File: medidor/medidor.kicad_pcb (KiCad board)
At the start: 2 copper layers, 55 x 80 mm, 23 parts, among them J1 Screw_Terminal_01x02, J2 Conn_01x01_Female, J3 Conn_01x01_Female, J4 Conn_01x06, J5 Screw_Terminal_01x02, U1 LTC1966CMS8PBF, U2 MCP6001U

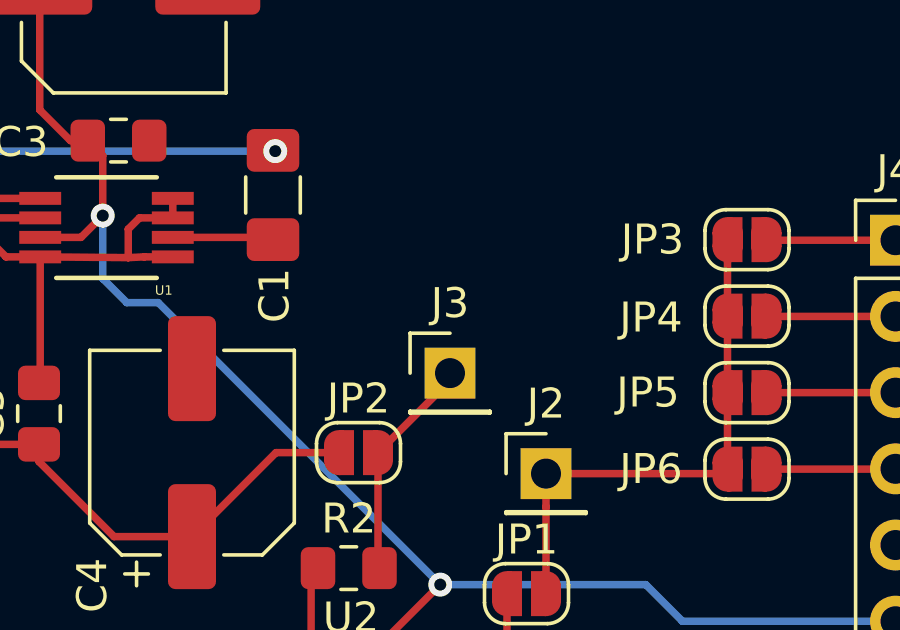
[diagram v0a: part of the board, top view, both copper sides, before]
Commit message: Se agregan cotas al PCB
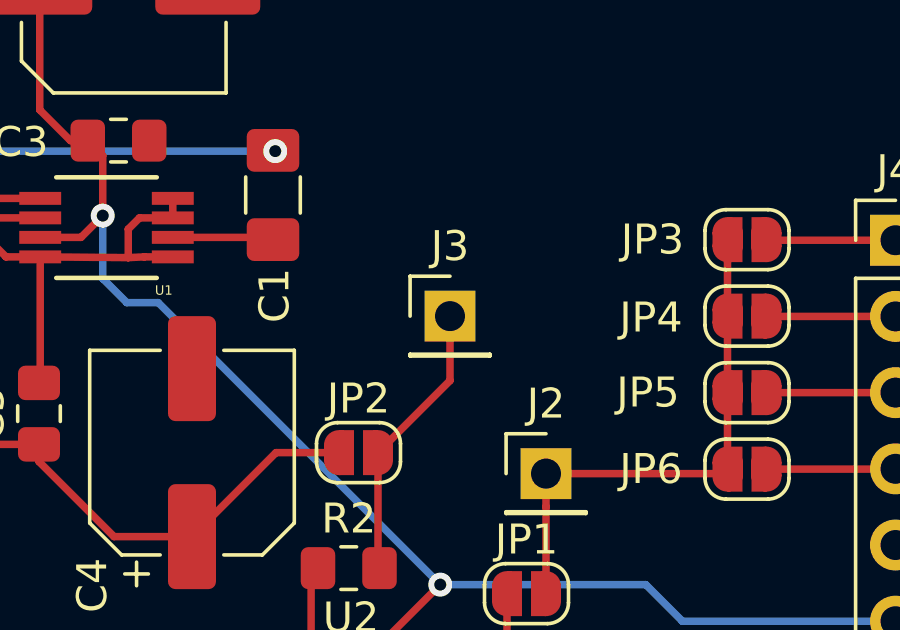
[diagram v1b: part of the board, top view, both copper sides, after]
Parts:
- moved J3 1.90 mm to (135.9, 93.5)
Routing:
- net /IN+_MCP6001: track 7.51 -> 9.41 mm
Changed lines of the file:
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@@
   (general
     (thickness 1.6)
-    (drawings 5)
+    (drawings 7)
     (tracks 94)
     (zones 0)
@@
   )
   (module Connector_PinHeader_2.54mm:PinHeader_1x01_P2.54mm_Vertical (layer F.Cu)
-    (at 135.875 95.35)
+    (at 135.875 93.45)
     (descr "Through hole straight pin header, 1x01, 2.54mm pitch, single row")
     (tags "Through hole pin header THT 1x01 2.54mm single row")
@@
       (rotate (xyz 0 0 0))
     )
+  )
+  (dimension 55 (width 0.15) (layer Dwgs.User)
+    (gr_text "55,000 mm" (at 127.5 43.7) (layer Dwgs.User)
+      (effects (font (size 1 1) (thickness 0.15)))
+    )
+    (feature1 (pts (xy 155 55) (xy 155 44.413579)))
+    (feature2 (pts (xy 100 55) (xy 100 44.413579)))
+    (crossbar (pts (xy 100 45) (xy 155 45)))
+    (arrow1a (pts (xy 155 45) (xy 153.873496 45.586421)))
+    (arrow1b (pts (xy 155 45) (xy 153.873496 44.413579)))
+    (arrow2a (pts (xy 100 45) (xy 101.126504 45.586421)))
+    (arrow2b (pts (xy 100 45) (xy 101.126504 44.413579)))
+  )
+  (dimension 80 (width 0.15) (layer Dwgs.User)
+    (gr_text "80,000 mm" (at 166.3 95 90) (layer Dwgs.User)
+      (effects (font (size 1 1) (thickness 0.15)))
+    )
+    (feature1 (pts (xy 155 55) (xy 165.586421 55)))
+    (feature2 (pts (xy 155 135) (xy 165.586421 135)))
+    (crossbar (pts (xy 165 135) (xy 165 55)))
+    (arrow1a (pts (xy 165 55) (xy 165.586421 56.126504)))
+    (arrow1b (pts (xy 165 55) (xy 164.413579 56.126504)))
+    (arrow2a (pts (xy 165 135) (xy 165.586421 133.873496)))
+    (arrow2b (pts (xy 165 135) (xy 164.413579 133.873496)))
   )
   (gr_text "ENTRADA TI" (at 136.8 73.65) (layer F.SilkS)
@@
   (segment (start 133.475 101.8) (end 133.525 101.85) (width 0.25) (layer F.Cu) (net 6))
   (segment (start 133.475 98) (end 133.475 101.8) (width 0.25) (layer F.Cu) (net 6))
-  (segment (start 135.875 95.6) (end 135.875 95.35) (width 0.25) (layer F.Cu) (net 6))
+  (segment (start 135.875 95.6) (end 135.875 93.45) (width 0.25) (layer F.Cu) (net 6))
   (segment (start 133.475 98) (end 135.875 95.6) (width 0.25) (layer F.Cu) (net 6))
   (segment (start 133.905 106.15) (end 136.575 106.15) (width 0.25) (layer F.Cu) (net 7))

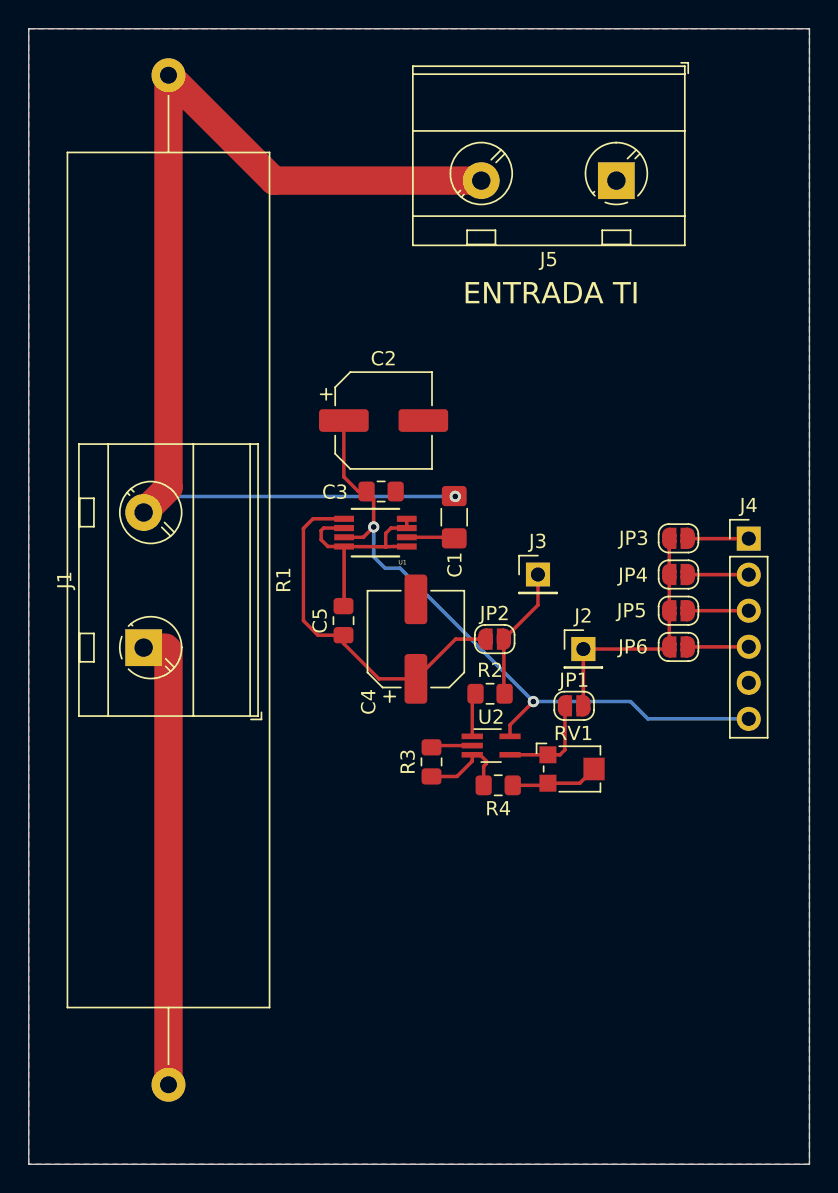
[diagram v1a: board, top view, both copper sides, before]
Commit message: Se agregan fiduciarios
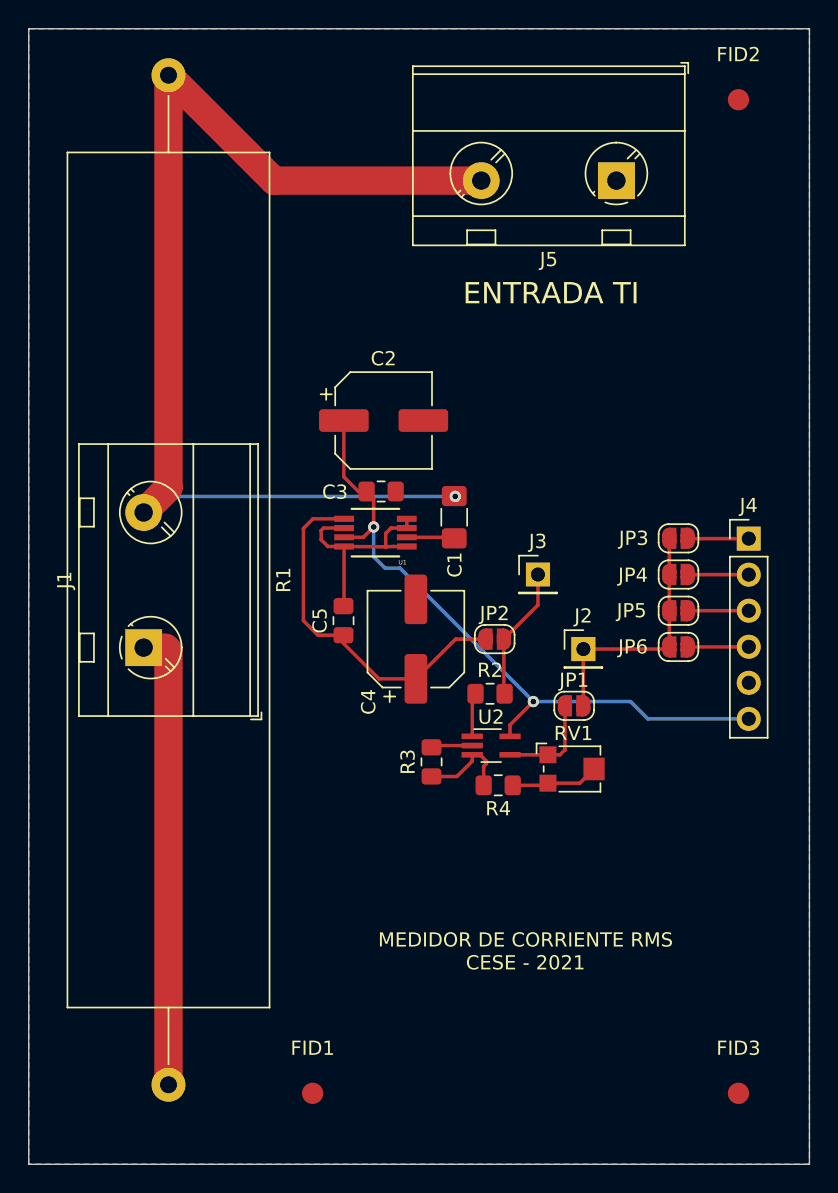
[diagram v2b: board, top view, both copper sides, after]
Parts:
- added FID1: Fiducial, Fiducial:Fiducial_1.5mm_Mask4.5mm, F.Cu at (120.0, 130.0)
- added FID2: Fiducial, Fiducial:Fiducial_1.5mm_Mask4.5mm, F.Cu at (150.0, 60.0)
- added FID3: Fiducial, Fiducial:Fiducial_1.5mm_Mask4.5mm, F.Cu at (150.0, 130.0)
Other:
- board text added: "MEDIDOR DE CORRIENTE RMS CESE - 2021"
- board text added: "NOTAS AL FABRICANTE"
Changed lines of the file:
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@@
   (general
     (thickness 1.6)
-    (drawings 7)
+    (drawings 9)
     (tracks 94)
     (zones 0)
-    (modules 23)
+    (modules 26)
     (nets 16)
   )
@@
     (add_net "Net-(R4-Pad1)")
     (add_net VDD)
+  )
+  (module Fiducial:Fiducial_1.5mm_Mask4.5mm (layer F.Cu)
+    (at 150 130)
+    (descr "Circular Fiducial, 1.5mm bare copper, 4.5mm soldermask opening")
+    (tags fiducial)
+    (attr smd)
+    (fp_text reference FID3 (at 0 -3.175) (layer F.SilkS)
+      (effects (font (size 1 1) (thickness 0.15)))
+    )
+    (fp_text value Fiducial (at 0 3.175) (layer F.Fab)
+      (effects (font (size 1 1) (thickness 0.15)))
+    )
+    (fp_circle (center 0 0) (end 2.5 0) (layer F.CrtYd) (width 0.05))
+    (fp_text user %R (at 0 0) (layer F.Fab)
+      (effects (font (size 0.4 0.4) (thickness 0.06)))
+    )
+    (fp_circle (center 0 0) (end 2.25 0) (layer F.Fab) (width 0.1))
+    (pad "" smd circle (at 0 0) (size 1.5 1.5) (layers F.Cu F.Mask)
+      (solder_mask_margin 1.5) (clearance 1.5))
+  )
+  (module Fiducial:Fiducial_1.5mm_Mask4.5mm (layer F.Cu)
+    (at 150 60)
+    (descr "Circular Fiducial, 1.5mm bare copper, 4.5mm soldermask opening")
+    (tags fiducial)
+    (attr smd)
+    (fp_text reference FID2 (at 0 -3.175) (layer F.SilkS)
+      (effects (font (size 1 1) (thickness 0.15)))
+    )
+    (fp_text value Fiducial (at 0 3.175) (layer F.Fab)
+      (effects (font (size 1 1) (thickness 0.15)))
+    )
+    (fp_circle (center 0 0) (end 2.5 0) (layer F.CrtYd) (width 0.05))
+    (fp_text user %R (at 0 0) (layer F.Fab)
+      (effects (font (size 0.4 0.4) (thickness 0.06)))
+    )
+    (fp_circle (center 0 0) (end 2.25 0) (layer F.Fab) (width 0.1))
+    (pad "" smd circle (at 0 0) (size 1.5 1.5) (layers F.Cu F.Mask)
+      (solder_mask_margin 1.5) (clearance 1.5))
+  )
+  (module Fiducial:Fiducial_1.5mm_Mask4.5mm (layer F.Cu)
+    (at 120 130)
+    (descr "Circular Fiducial, 1.5mm bare copper, 4.5mm soldermask opening")
+    (tags fiducial)
+    (attr smd)
+    (fp_text reference FID1 (at 0 -3.175) (layer F.SilkS)
+      (effects (font (size 1 1) (thickness 0.15)))
+    )
+    (fp_text value Fiducial (at 0 3.175) (layer F.Fab)
+      (effects (font (size 1 1) (thickness 0.15)))
+    )
+    (fp_circle (center 0 0) (end 2.5 0) (layer F.CrtYd) (width 0.05))
+    (fp_text user %R (at 0 0) (layer F.Fab)
+      (effects (font (size 0.4 0.4) (thickness 0.06)))
+    )
+    (fp_circle (center 0 0) (end 2.25 0) (layer F.Fab) (width 0.1))
+    (pad "" smd circle (at 0 0) (size 1.5 1.5) (layers F.Cu F.Mask)
+      (solder_mask_margin 1.5) (clearance 1.5))
   )
   (module TerminalBlock_MetzConnect:TerminalBlock_MetzConnect_Type703_RT10N02HGLU_1x02_P9.52mm_Horizontal (layer F.Cu)
@@
       (rotate (xyz 0 0 0))
     )
+  )
+  (gr_text "MEDIDOR DE CORRIENTE RMS\nCESE - 2021\n" (at 135 120) (layer F.SilkS)
+    (effects (font (size 1 1) (thickness 0.15)))
+  )
+  (gr_text "NOTAS AL FABRICANTE\n" (at 180 70) (layer Dwgs.User)
+    (effects (font (size 1 1) (thickness 0.15)))
   )
   (dimension 55 (width 0.15) (layer Dwgs.User)
@@
   (segment (start 117.27 65.7) (end 109.845 58.275) (width 2) (layer F.Cu) (net 15))
   (segment (start 131.88 65.7) (end 117.27 65.7) (width 2) (layer F.Cu) (net 15))
-  (zone (net 2) (net_name GND) (layer B.Cu) (hatch edge 0.508)
+  (zone (net 2) (net_name GND) (layer F.Cu) (hatch edge 0.508)
     (connect_pads (clearance 0.508))
     (min_thickness 0.254)
@@
     )
   )
-  (zone (net 2) (net_name GND) (layer F.Cu) (hatch edge 0.508)
+  (zone (net 2) (net_name GND) (layer B.Cu) (hatch edge 0.508)
     (connect_pads (clearance 0.508))
     (min_thickness 0.254)

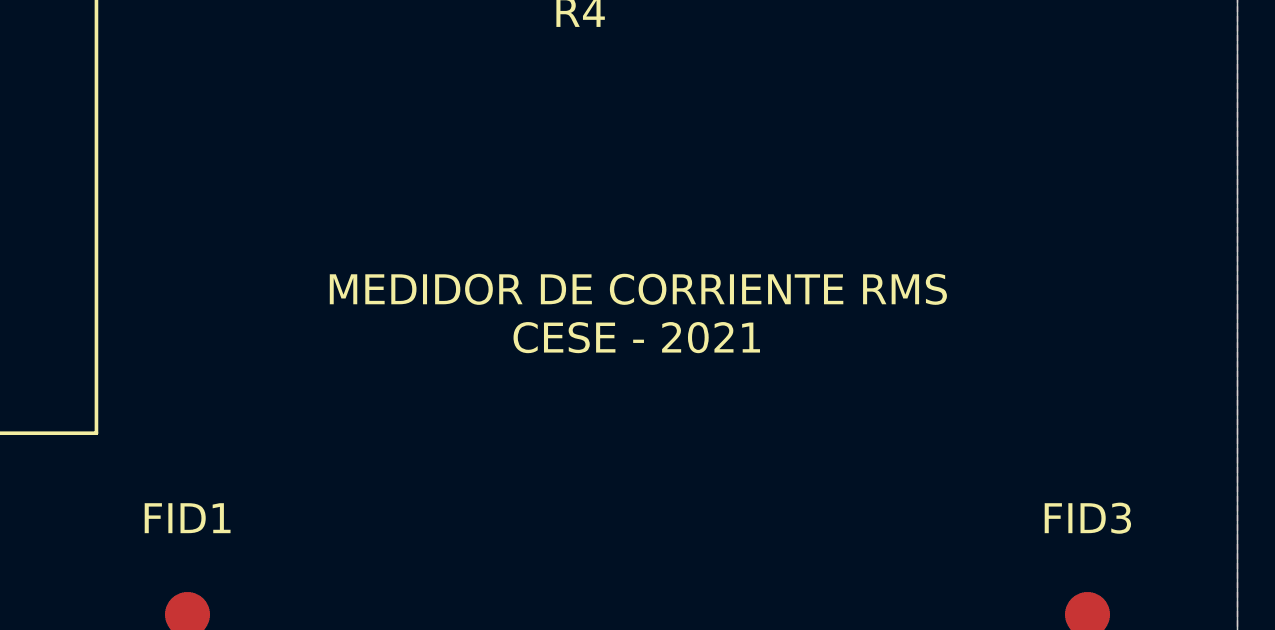
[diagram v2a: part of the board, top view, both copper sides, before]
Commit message: Se agrega leyenda en serigrafia
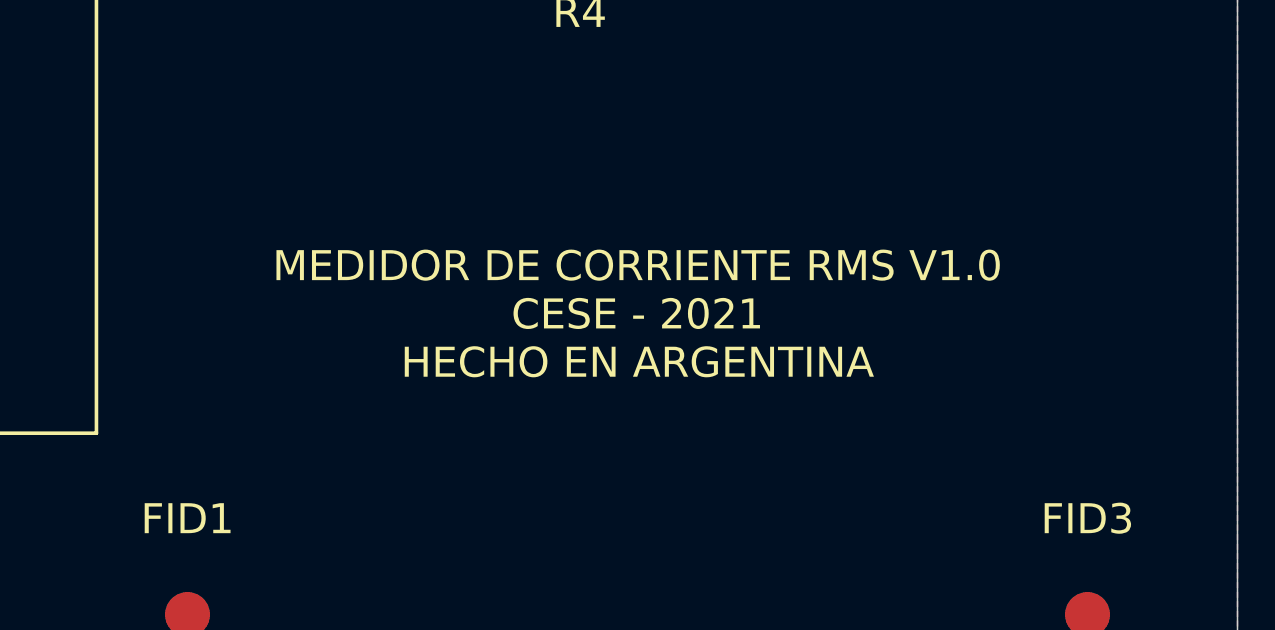
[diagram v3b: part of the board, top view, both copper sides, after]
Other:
- board text added: "MEDIDOR DE CORRIENTE RMS V1.0 CESE - 2021 HECHO EN ARGENTINA"
- board text removed: "MEDIDOR DE CORRIENTE RMS CESE - 2021"
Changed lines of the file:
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@@
     )
   )
-  (gr_text "MEDIDOR DE CORRIENTE RMS\nCESE - 2021\n" (at 135 120) (layer F.SilkS)
+  (gr_text "MEDIDOR DE CORRIENTE RMS V1.0\nCESE - 2021\nHECHO EN ARGENTINA\n" (at 135 120) (layer F.SilkS)
     (effects (font (size 1 1) (thickness 0.15)))
   )
@@
   (segment (start 122.2 82.6) (end 122.2 86.575) (width 0.25) (layer F.Cu) (net 3))
   (segment (start 133.905 104.045) (end 135.55 102.4) (width 0.25) (layer F.Cu) (net 3))
-  (via (at 135.55 102.4) (size 0.8) (drill 0.4) (layers F.Cu B.Cu) (net 3))
+  (via (at 135.55 102.4) (size 0.8) (drill 0.4) (layers F.Cu B.Cu) (net 3) (status 1000000))
   (segment (start 133.905 104.85) (end 133.905 104.045) (width 0.25) (layer F.Cu) (net 3))
   (segment (start 135.55 102.4) (end 126.15 93) (width 0.25) (layer B.Cu) (net 3))

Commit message: Se agregan datos en rotulo
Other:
- board text added: "NOTAS AL FABRICANTE VIAS: 0.8mm VIA DRILL: 0.4mm PISTAS: 0.25mm Y 2 mm"
- board text removed: "NOTAS AL FABRICANTE"
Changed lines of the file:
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@@
   )
   (page A4)
+  (title_block
+    (title "MEDIDOR DE CORRIENTE RMS")
+    (date 2021-04-13)
+    (company "Ing. Milton Eduardo Sosa")
+    (comment 1 "OHL Licence")
+  )
   (layers
     (0 F.Cu signal)
@@
   (setup
     (last_trace_width 0.25)
+    (user_trace_width 0.25)
+    (user_trace_width 2)
     (trace_clearance 0.2)
     (zone_clearance 0.508)
@@
     (via_min_size 0.4)
     (via_min_drill 0.3)
+    (user_via 0.8 0.4)
     (uvia_size 0.3)
     (uvia_drill 0.1)
@@
     (effects (font (size 1 1) (thickness 0.15)))
   )
-  (gr_text "NOTAS AL FABRICANTE\n" (at 180 70) (layer Dwgs.User)
+  (gr_text "NOTAS AL FABRICANTE\nVIAS: 0.8mm \nVIA DRILL: 0.4mm\nPISTAS: 0.25mm Y 2 mm\n" (at 180 70) (layer Dwgs.User)
     (effects (font (size 1 1) (thickness 0.15)))
   )
